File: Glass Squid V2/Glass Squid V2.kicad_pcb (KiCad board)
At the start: 2 copper layers, 93.8 x 34.8 mm, 29 parts, among them J1 Conn_01x16, J2 Conn_01x12, J3 SM04B-GHS-TB, J4 Qwiic_Vertical, J5 B2B-XH-A-GU, J6 B2B-XH-A-GU, J7 Conn_01x02, J9 Conn_01x03, Q1 AOSS32136C, U1 DRV8871DDA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

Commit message: V1 of Float Boards ... most likely :)
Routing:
- net /SDA: track 75.5 -> 79.1 mm

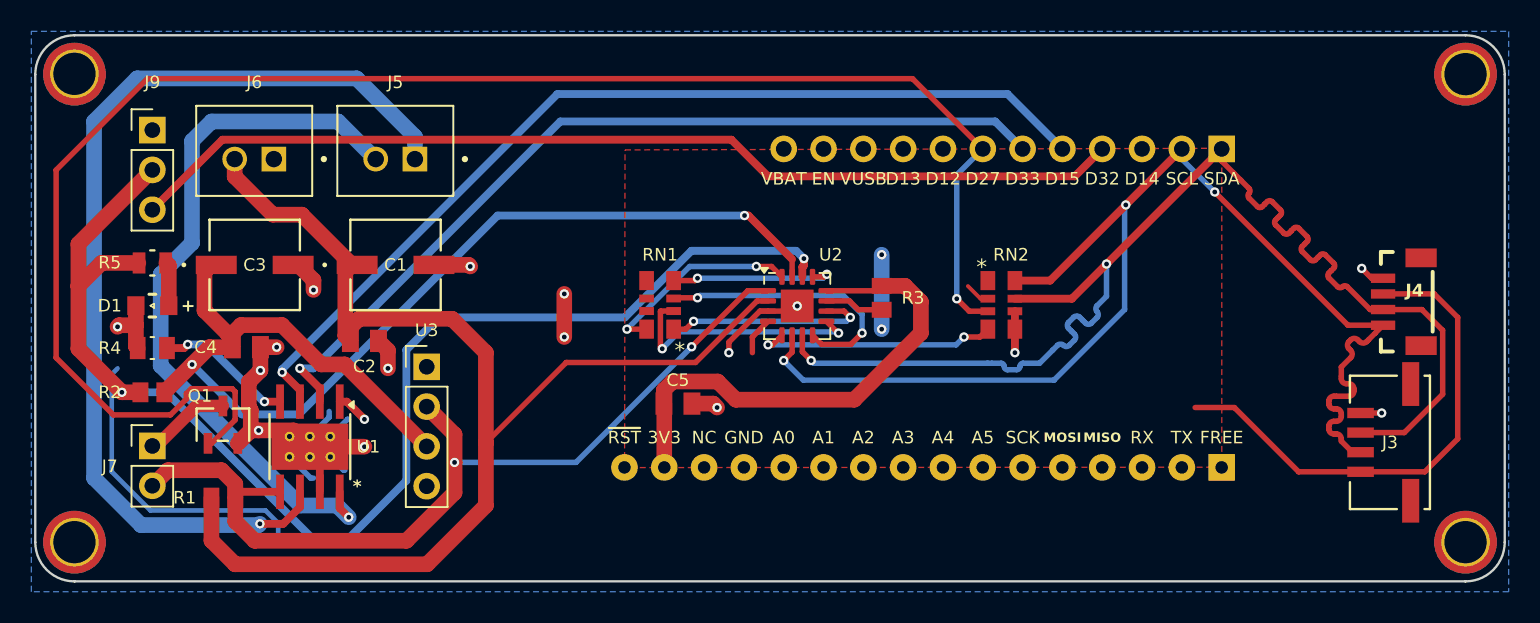
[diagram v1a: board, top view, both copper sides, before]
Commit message: Created .zip files and ordered the boards.
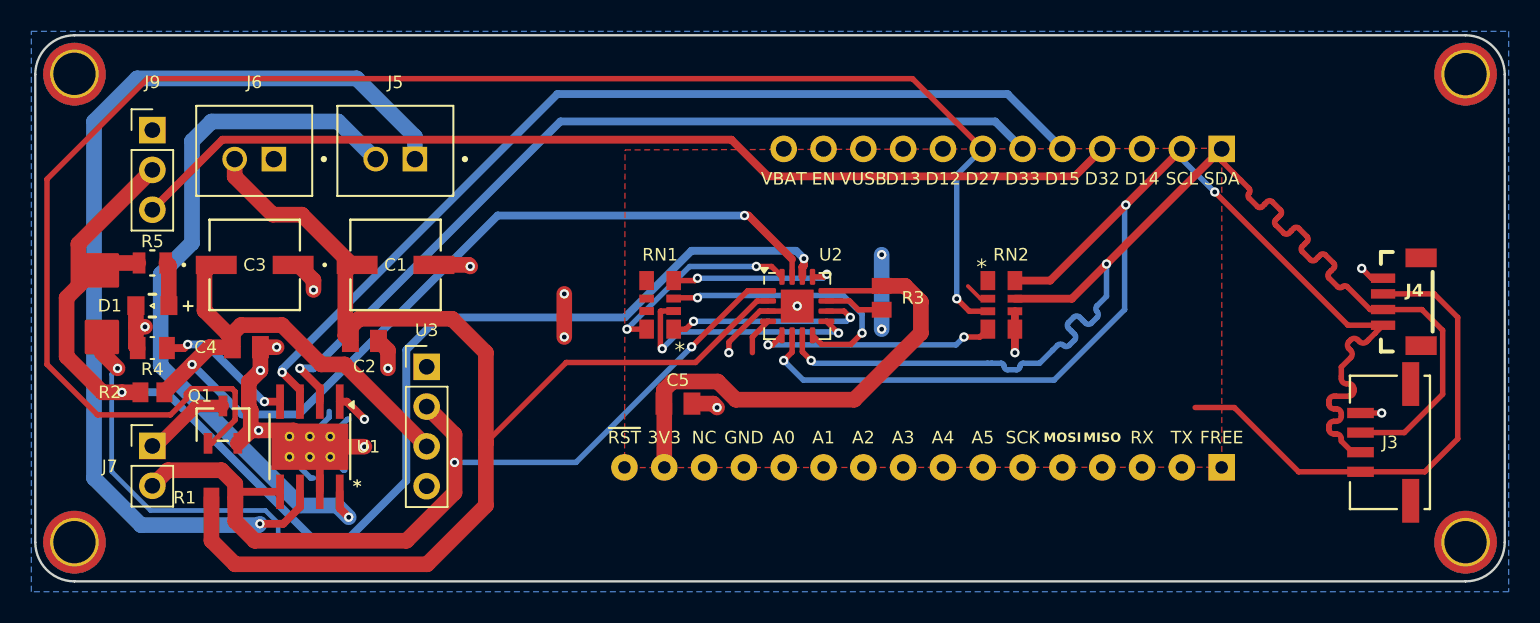
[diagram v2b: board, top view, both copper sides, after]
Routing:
- net GND: track 73.9 -> 75.7 mm, vias 17 -> 18
- net +5V: track 84.3 -> 85.6 mm
- net D27: track 106.0 -> 107.0 mm
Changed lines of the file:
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@@
 		)
 		(pad_to_mask_clearance 0)
-		(solder_mask_min_width 0.25)
 		(allow_soldermask_bridges_in_footprints no)
 		(pcbplotparams
@@
 			(plot_on_all_layers_selection 0x0000000_00000000)
 			(disableapertmacros no)
-			(usegerberextensions no)
+			(usegerberextensions yes)
 			(usegerberattributes no)
 			(usegerberadvancedattributes no)
@@
 			(plotinvisibletext no)
 			(sketchpadsonfab no)
-			(subtractmaskfromsilk no)
+			(subtractmaskfromsilk yes)
 			(outputformat 1)
 			(mirror no)
-			(drillshape 1)
+			(drillshape 0)
 			(scaleselection 1)
-			(outputdirectory "")
+			(outputdirectory "./")
 		)
 	)
@@
 		(at 99.9708 99.204833)
 		(property "Reference" "R4"
-			(at -2.7208 0 0)
+			(at 0 1.35 0)
 			(layer "F.SilkS")
 			(effects
@@
 		(tags "CHP0805AFX-2200ELF ")
 		(property "Reference" "R5"
-			(at -2.7208 -0.026867 0)
+			(at 0 -1.376867 0)
 			(unlocked yes)
 			(layer "F.SilkS")
@@
 		)
 	)
+	(gr_rect
+		(start 95.75 93.25)
+		(end 97.75 95.25)
+		(stroke
+			(width 0.2)
+			(type solid)
+		)
+		(fill solid)
+		(layer "F.Cu")
+		(net 39)
+	)
+	(gr_rect
+		(start 95.75 97.5)
+		(end 97.75 99.5)
+		(stroke
+			(width 0.2)
+			(type solid)
+		)
+		(fill solid)
+		(layer "F.Cu")
+		(net 13)
+	)
+	(gr_rect
+		(start 95.75 97.5)
+		(end 97.75 99.5)
+		(stroke
+			(width 0.2)
+			(type solid)
+		)
+		(fill solid)
+		(layer "F.Mask")
+	)
+	(gr_rect
+		(start 95.75 93.25)
+		(end 97.75 95.25)
+		(stroke
+			(width 0.2)
+			(type solid)
+		)
+		(fill solid)
+		(layer "F.Mask")
+	)
+	(gr_line
+		(start 122 96.5)
+		(end 92.5 96.5)
+		(stroke
+			(width 0.1)
+			(type default)
+		)
+		(layer "Dwgs.User")
+	)
 	(gr_line
 		(start 119.9708 105.15)
@@
 	)
 	(segment
+		(start 99.5 97.85)
+		(end 99.0208 97.85)
+		(width 1)
+		(layer "F.Cu")
+		(net 13)
+	)
+	(segment
 		(start 110.0208 105.5)
 		(end 113.5 105.5)
@@
 	)
 	(segment
-		(start 140.7875 96.85)
-		(end 141.1125 96.525)
-		(width 0.35)
+		(start 99.0208 97.85)
+		(end 98.9208 97.75)
+		(width 1)
 		(layer "F.Cu")
 		(net 13)
 	)
 	(segment
-		(start 98.9208 97.75)
-		(end 97.85 97.75)
-		(width 1)
+		(start 140.7875 96.85)
+		(end 141.1125 96.525)
+		(width 0.35)
 		(layer "F.Cu")
 		(net 13)
@@
 	)
 	(segment
-		(start 97.85 97.75)
-		(end 97.75 97.85)
-		(width 1)
-		(layer "F.Cu")
-		(net 13)
-	)
-	(segment
 		(start 178.400001 103.349999)
 		(end 177.049999 103.349999)
@@
 	)
 	(segment
+		(start 96.75 98.5)
+		(end 96.75 99.5)
+		(width 1)
+		(layer "F.Cu")
+		(net 13)
+	)
+	(segment
 		(start 110.6558 108.375)
 		(end 110.6558 106.135)
@@
 	)
 	(segment
+		(start 96.75 99.5)
+		(end 97.75 100.5)
+		(width 1)
+		(layer "F.Cu")
+		(net 13)
+	)
+	(segment
 		(start 98.9208 96.5)
 		(end 98.9208 97.75)
@@
 	)
 	(via
+		(at 97.75 100.5)
+		(size 0.6)
+		(drill 0.3)
+		(layers "F.Cu" "B.Cu")
+		(net 13)
+	)
+	(via
 		(at 107.9 99.15)
 		(size 0.6)
@@
 	)
 	(via
-		(at 97.75 97.85)
+		(at 99.5 97.85)
 		(size 0.6)
 		(drill 0.3)
@@
 	)
 	(segment
-		(start 97.48 103.47)
-		(end 93.83 99.82)
+		(start 105.25 103.79)
+		(end 103.7524 105.2876)
 		(width 0.35)
 		(layer "F.Cu")
@@
 	)
 	(segment
-		(start 101.123984 103.47)
-		(end 97.48 103.47)
+		(start 103.7524 105.2876)
+		(end 103.520799 105.2876)
 		(width 0.35)
 		(layer "F.Cu")
@@
 	)
 	(segment
-		(start 99.66 82.02)
-		(end 148.47 82.02)
+		(start 96.47 103.47)
+		(end 101.123984 103.47)
 		(width 0.35)
 		(layer "F.Cu")
@@
 	)
 	(segment
-		(start 93.83 87.85)
-		(end 99.66 82.02)
+		(start 105.0606 101.8)
+		(end 105.25 101.9894)
 		(width 0.35)
 		(layer "F.Cu")
@@
 	)
 	(segment
-		(start 102.45 101.8)
-		(end 102.14 102.11)
+		(start 152.95 86.5)
+		(end 148.47 82.02)
 		(width 0.35)
 		(layer "F.Cu")
@@
 	)
 	(segment
-		(start 105.0606 101.8)
-		(end 102.45 101.8)
+		(start 93.25 88.43)
+		(end 93.25 100.25)
 		(width 0.35)
 		(layer "F.Cu")
@@
 	)
 	(segment
-		(start 103.520799 105.2876)
-		(end 103.7524 105.2876)
+		(start 148.47 82.02)
+		(end 99.66 82.02)
 		(width 0.35)
 		(layer "F.Cu")
@@
 	)
 	(segment
-		(start 102.14 102.453984)
-		(end 101.123984 103.47)
+		(start 105.25 101.9894)
+		(end 105.25 103.79)
 		(width 0.35)
 		(layer "F.Cu")
@@
 	)
 	(segment
-		(start 148.47 82.02)
-		(end 152.95 86.5)
+		(start 101.123984 103.47)
+		(end 102.14 102.453984)
 		(width 0.35)
 		(layer "F.Cu")
@@
 	)
 	(segment
-		(start 105.25 103.79)
-		(end 105.25 101.9894)
+		(start 102.14 102.11)
+		(end 102.45 101.8)
 		(width 0.35)
 		(layer "F.Cu")
@@
 	)
 	(segment
-		(start 103.7524 105.2876)
-		(end 105.25 103.79)
+		(start 93.25 100.25)
+		(end 96.47 103.47)
 		(width 0.35)
 		(layer "F.Cu")
@@
 	)
 	(segment
-		(start 93.83 99.82)
-		(end 93.83 87.85)
+		(start 99.66 82.02)
+		(end 93.25 88.43)
 		(width 0.35)
 		(layer "F.Cu")
@@
 	)
 	(segment
-		(start 105.25 101.9894)
-		(end 105.0606 101.8)
+		(start 102.14 102.453984)
+		(end 102.14 102.11)
 		(width 0.35)
 		(layer "F.Cu")
@@
 	)
 	(segment
-		(start 102.14 102.11)
-		(end 102.14 102.453984)
+		(start 102.45 101.8)
+		(end 105.0606 101.8)
 		(width 0.35)
 		(layer "F.Cu")
@@
 	)
 	(segment
-		(start 99.9708 87.84)
-		(end 95.25 92.5608)
+		(start 98.026867 102.026867)
+		(end 96.776867 102.026867)
+		(width 1)
+		(layer "F.Cu")
+		(net 39)
+	)
+	(segment
+		(start 95.25 92.5608)
+		(end 95.25 95.25)
 		(width 1)
 		(layer "F.Cu")
@@
 	)
 	(segment
-		(start 95.25 92.5608)
-		(end 95.25 95.25)
+		(start 99.9708 87.84)
+		(end 95.25 92.5608)
 		(width 1)
 		(layer "F.Cu")
@@
 	)
 	(segment
-		(start 95.25 99.25)
-		(end 95.25 95.25)
-		(width 1)
-		(layer "F.Cu")
-		(net 39)
-	)
-	(segment
-		(start 98.026867 102.026867)
-		(end 95.25 99.25)
+		(start 94.5 99.75)
+		(end 94.5 96)
 		(width 1)
 		(layer "F.Cu")
@@
 		(width 1)
 		(layer "F.Cu")
+		(net 39)
+	)
+	(segment
+		(start 96.776867 102.026867)
+		(end 94.5 99.75)
+		(width 1)
+		(layer "F.Cu")
+		(net 39)
+	)
+	(segment
+		(start 94.5 96)
+		(end 95.25 95.25)
+		(width 1)
+		(layer "F.Cu")
